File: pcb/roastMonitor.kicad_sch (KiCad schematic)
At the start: 43 parts, among them J1 USB_C_Receptacle_USB2.0_16P, J2 Conn_01x02, J3 Conn_01x02, J4 Conn_01x04, J5 Conn_01x04, U1 REF3040, U2 USBLC6-2SC6, U3 OPA2333xxD, U4 CH32X033F8P6, U5 MCP9701A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

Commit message: Update PCB
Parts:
- C1, C18, C2, C20, C21, C22, C3, C4, C5, C6, C7: footprint (none) -> Capacitor_SMD:C_0603_1608Metric
- C19: footprint (none) -> Capacitor_SMD:C_1206_3216Metric
- D1: footprint (none) -> LED_SMD:LED_0603_1608Metric
- F1: footprint (none) -> Fuse:Fuse_1812_4532Metric
- J1: footprint (none) -> Connector_USB:USB_C_Receptacle_GCT_USB4105-xx-A_16P_TopMnt_Horizontal
- J2, J3: footprint (none) -> TerminalBlock_MetzConnect:TerminalBlock_MetzConnect_Type067_RT01902HDWC_1x02_P10.00mm_Horizontal
- J4, J5: footprint (none) -> Connector_JST:JST_PH_B4B-PH-K_1x04_P2.00mm_Vertical
- R1, R2, R25, R26, R27, R28, R29, R3, R30, R6: footprint (none) -> Resistor_SMD:R_0603_1608Metric
- R4, R5: value 100k -> 100k±0.1%; footprint (none) -> Resistor_SMD:R_0603_1608Metric
- TP3, TP4, TP5, TP6: footprint (none) -> TestPoint:TestPoint_Pad_D1.5mm
- U3, U6: footprint (none) -> Package_SO:SOIC-8_3.9x4.9mm_P1.27mm
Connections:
- no-connect marks 2 -> 9

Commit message: Update PCB
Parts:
- removed C18, C21, C22, C4, C5, C7: 100n, Capacitor_SMD:C_0603_1608Metric, symbol Device:C
- removed C19: 4.7u, Capacitor_SMD:C_1206_3216Metric, symbol Device:C
- removed F1: Polyfuse, Fuse:Fuse_1812_4532Metric, symbol Device:Polyfuse
- removed J1: USB_C_Receptacle_USB2.0_16P, Connector_USB:USB_C_Receptacle_GCT_USB4105-xx-A_16P_TopMnt_Horizontal, symbol Connector:USB_C_Receptacle_USB2.0_16P
- removed J3: Conn_01x02, TerminalBlock_MetzConnect:TerminalBlock_MetzConnect_Type067_RT01902HDWC_1x02_P10.00mm_Horizontal, symbol Connector_Generic:Conn_01x02
- removed J4, J5: Conn_01x04, Connector_JST:JST_PH_B4B-PH-K_1x04_P2.00mm_Vertical, symbol Connector_Generic:Conn_01x04
- removed R1, R2: 5.1k, Resistor_SMD:R_0603_1608Metric, symbol Device:R
- removed R25, R26, R29, R30: 22, Resistor_SMD:R_0603_1608Metric, symbol Device:R
- removed R27: 10k, Resistor_SMD:R_0603_1608Metric, symbol Device:R
- removed S1, S2: SKRPACE010, private:SW_SKRPACE010, symbol private:SKRPACE010
- removed TP3, TP4, TP5, TP6: TestPoint, TestPoint:TestPoint_Pad_D1.5mm, symbol Connector:TestPoint
- removed U2: USBLC6-2SC6, Package_TO_SOT_SMD:SOT-23-6, symbol Power_Protection:USBLC6-2SC6
- removed U4: CH32X033F8P6, private:TSSOP-20_L6.5-W4.4-P0.65-LS6.4-BL, symbol private:CH32X033F8P6
- removed U6: OPA2333xxD, Package_SO:SOIC-8_3.9x4.9mm_P1.27mm, symbol Amplifier_Operational:OPA2333xxD
- added C23: 1u, Capacitor_SMD:C_0603_1608Metric, symbol Device:C
- added C25: 100n, Capacitor_SMD:C_0603_1608Metric, symbol Device:C
- added D2: D, Diode_SMD:D_SOD-123F, symbol Device:D
- added H1, H2, H3, H4: MountingHole, MountingHole:MountingHole_3.2mm_M3, symbol Mechanical:MountingHole
- added U6: XIAO-ESP32-C3-DIP, private:XIAO-ESP32-C3-DIP, symbol private:XIAO-ESP32-C3-DIP
- J2: footprint TerminalBlock_MetzConnect:TerminalBlock_MetzConnect_Type067_RT01902HDWC_1x02_P10.00mm_Horizontal -> TerminalBlock_RND:TerminalBlock_RND_205-00241_1x02_P10.16mm_Horizontal
- R4, R5: value 100k±0.1% -> 1k±0.1%
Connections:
- net +5V: now also C25.1, U6.14 (VBUS)
- net GND: now also C23.2, C25.2, U6.13 (GND)
- net Vref: now also U6.1 (GPIO2_A0_D0)
- net Vthermo1: now also D2.2 (A), U6.3 (GPIO4_A2_D2)
- net at R6.1: now also U5.2 (V_{OUT})
- net Vtemp: now reaches R6.2
- net Vtemp: now also C23.1, U6.2 (GPIO3_A1_D1); no longer U5.2 (V_{OUT})
- new net: D2.1 (K), U6.12 (3V3)
- no-connect marks 9 -> 8
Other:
- removed sheet amp1
- added sheet mcu (muc.kicad_sch)
- moved on the sheet: C3, D1, R28

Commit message: update value
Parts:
- R4: value 1k±0.1% -> 680±0.1%
- R5: value 1k±0.1% -> 100±0.1%
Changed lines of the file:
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@@
 			)
 		)
-		(property "Value" "1k±0.1%"
+		(property "Value" "680±0.1%"
 			(at 72.39 134.6199 0)
 			(show_name no)
@@
 			)
 		)
-		(property "Value" "1k±0.1%"
+		(property "Value" "100±0.1%"
 			(at 72.39 147.3199 0)
 			(show_name no)

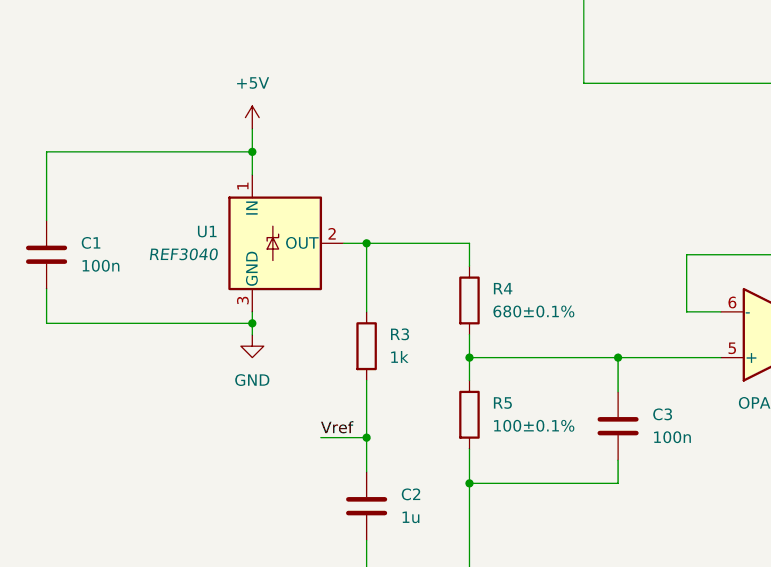
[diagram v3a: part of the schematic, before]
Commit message: Update register values
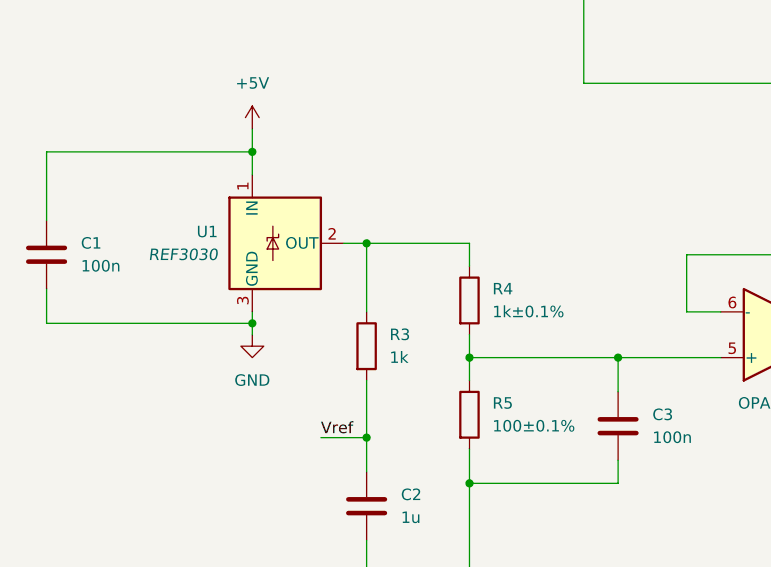
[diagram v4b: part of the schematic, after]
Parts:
- R4: value 680±0.1% -> 1k±0.1%
- U1: value REF3040 -> REF3030
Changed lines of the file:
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@@
 			)
 		)
-		(property "Value" "680±0.1%"
+		(property "Value" "1k±0.1%"
 			(at 72.39 134.6199 0)
 			(show_name no)
@@
 			)
 		)
-		(property "Value" "REF3040"
+		(property "Value" "REF3030"
 			(at 41.91 128.2699 0)
 			(show_name no)
